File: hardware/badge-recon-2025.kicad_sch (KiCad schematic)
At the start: 73 parts, among them J1 Battery, J3 MAGSPOOF, J4 MAGSPOOF, P1 USB_C_Plug_USB2.0, Q1 DMG3415U-7, SW1 SW_Push, SW2 SW_Push, SW3 ON, SW4 SOURCE MAG, SW5 SW_Push, SW6 SW_Push, SW7 RESET, U1 PN7150B0HN_C11002E-PN7150B0HN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, U2 RP2040, U4 AP2112K-3.3, U6 W25Q16JV, U7 TC4424, Y1 27.12Mhz, Y2 12Mhz

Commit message: feat(hw): add oled in schematic
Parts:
- removed J1: Battery, Connector_PinHeader_2.54mm:PinHeader_1x02_P2.54mm_Vertical, symbol Connector:Screw_Terminal_01x02
- removed J3, J4: MAGSPOOF, Connector_PinHeader_2.54mm:PinHeader_1x02_P2.54mm_Vertical, symbol Connector_Generic:Conn_01x02
- added BT1, BT2: Battery_Cell, Battery:BatteryHolder_Keystone_2466_1xAAA, symbol Device:Battery_Cell
- added J5: OLED, Library:Display OLED 128 x32, symbol Connector:Screw_Terminal_01x04
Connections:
- net +3V3: now also J5.3 (Pin_3)
- net +BATT: now also BT2.2 (+)
- net GND: now also BT1.1 (-), J5.4 (Pin_4)
- net SCL: now also J5.2 (Pin_2)
- net SDA: now also J5.1 (Pin_1)
- net ACK_CTS: no longer names the net of U2.13 (GPIO10)
- net B_ADC: no longer names the net of U2.38 (GPIO26_ADC0)
- net CIPO_TX: no longer names the net of U2.11 (GPIO8)
- net COPI_RTS: no longer names the net of U2.14 (GPIO11)
- net CS_RX: no longer names the net of U2.12 (GPIO9)
- net LED1: no longer names the net of U2.39 (GPIO27_ADC1)
- net SWCLK: no longer names the net of U2.24 (SWCLK)
- net SWDIO: no longer names the net of U2.25 (SWD)
- new net: BT1.2 (+), BT2.1 (-)
- no-connect marks 14 -> 25
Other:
- note added: "BATTERY 2 AAA"
- note added: "OLED"
- note removed: "Missing to define which battery will be used, if 3 AAA battery or 2 Battery AA"

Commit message: feat(Hw):Update_BOM
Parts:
- removed BT1, BT2: Battery_Cell, Battery:BatteryHolder_Keystone_2466_1xAAA, symbol Device:Battery_Cell
- added J3: Battery, Footprint:BAT-TH_BH-AAA-A1AJ024, symbol Connector:Screw_Terminal_01x02
- C30, C31: LCSC# C561174 -> C107035; manf# C0603C121J5GAC -> (none)
- C34: LCSC# C466781 -> C96446; manf# C0603X5R106M160NT -> (none)
- JP1: now not fitted
- L3: manf# CONUFL001-SMD -> CONUFL001-SMD-T
- L4: footprint BomberCat:Coil_30t_30mm_0.2_0.2_0.6_0.3 -> Footprints:Coil_30t_30mm_0.2_0.2_0.6_0.3
- P1: LCSC# C2987386 -> C393939; manf# TYPE-C-31-M-31 -> (none)
- R1, R2, R20: LCSC# C169849 -> C2930027; manf# ERJ3GEYJ103V -> (none)
- R14, R21, R22: manf# WR06X104JTL -> (none)
- R4, R5: LCSC# C191782 -> C23186; manf# ERJ3RBD5101V -> (none)
- SW1, SW2, SW5, SW6: footprint (none) -> Button_Switch_SMD:SW_SPST_TL3342; LCSC# (none) -> C318889
- SW3: footprint BomberCat:JS102011SAQN -> Footprints:JS102011SAQN
- SW4: footprint BomberCat:JS202011CQN -> Footprints:JS202011CQN
- SW7: LCSC# C2886897 -> C318889
- U1: LCSC# C11002 -> C702907; manf# PN7150B0HN -> PN7150B0HN/C11002E
- U2: footprint BomberCat:RP2040-QFN-56 -> Footprints:RP2040-QFN-56
- U6: footprint BomberCat:W25Q16JVUUIQ -> Footprints:W25Q16JVUUIQ
- U7: LCSC# C636876 -> C44150
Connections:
- net +BATT: now also J3.2 (Pin_2)
- net GND: now also J3.1 (Pin_1)
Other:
- note removed: "BATTERY 2 AAA"

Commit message: feat(Hw):Init_Floorplan
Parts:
- J3: footprint Footprint:BAT-TH_BH-AAA-A1AJ024 -> Footprints:BAT-TH_BH-AAA-A1AJ024
- J5: footprint Library:Display OLED 128 x32 -> Footprints:Display OLED 128 x32
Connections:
- net CLK: no longer names the net of U1.40 (CLK_REQ)
- net GPIO1: no longer names the net of U2.28 (GPIO17)
- no-connect marks 25 -> 27
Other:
- moved on the sheet: C3, C4, C5, C6, C7, C8, C9, R1, R2, R21, R22, SW6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

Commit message: feat(Hw):Update_BOM
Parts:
- C23, C24: LCSC# C519403 -> C519507
- C25, C26: LCSC# (none) -> C107096
- C27, C28: LCSC# (none) -> C7503509
- F1: value 0.5A -> 0.75A; footprint Fuse:Fuse_0805_2012Metric -> Fuse:Fuse_0603_1608Metric; LCSC# - -> C182438; manf# MFU0805FF00500P100 -> (none)
- L3: manf# CONUFL001-SMD-T -> (none); now not fitted
- R18, R19: LCSC# C482832 -> C425452
- SW3: footprint Footprints:JS102011SAQN -> Footprints:MSK12C02; LCSC# - -> C431540; manf# JS102011SAQN -> (none)
- SW4: LCSC# (none) -> C5149820
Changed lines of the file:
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@@
 			)
 		)
+		(property "LCSC#" "C5149820"
+			(at 348.107 26.543 0)
+			(effects
+				(font
+					(size 1.27 1.27)
+				)
+				(hide yes)
+			)
+		)
 		(pin "1"
 		)
@@
 			)
 		)
-		(property "Footprint" "Footprints:JS102011SAQN"
+		(property "Footprint" "Footprints:MSK12C02"
 			(at 97.663 251.968 0)
 			(effects
@@
 			)
 		)
-		(property "LCSC#" "-"
+		(property "LCSC#" "C431540"
 			(at 97.663 251.968 0)
 			(effects
@@
 			)
 		)
-		(property "manf#" "JS102011SAQN"
+		(property "manf#" ""
 			(at 97.663 251.968 0)
 			(effects
@@
 			)
 		)
-		(property "LCSC#" "C482832"
+		(property "LCSC#" "C425452"
 			(at 205.232 52.07 0)
 			(effects
@@
 			)
 		)
-		(property "LCSC#" "C482832"
+		(property "LCSC#" "C425452"
 			(at 205.359 59.69 0)
 			(effects
@@
 			)
 		)
+		(property "LCSC#" "C7503509"
+			(at 184.15 42.926 0)
+			(effects
+				(font
+					(size 1.27 1.27)
+				)
+				(hide yes)
+			)
+		)
 		(pin "1"
 		)
@@
 			)
 		)
-		(property "Value" "0.5A"
+		(property "Value" "0.75A"
 			(at 51.308 233.8324 0)
 			(effects
@@
 			)
 		)
-		(property "Footprint" "Fuse:Fuse_0805_2012Metric"
+		(property "Footprint" "Fuse:Fuse_0603_1608Metric"
 			(at 51.308 236.22 0)
 			(effects
@@
 			)
 		)
-		(property "manf#" "MFU0805FF00500P100"
+		(property "manf#" ""
 			(at 51.308 236.22 0)
 			(effects
@@
 			)
 		)
-		(property "LCSC#" "-"
+		(property "LCSC#" "C182438"
 			(at 51.308 236.22 0)
 			(effects
@@
 			)
 		)
-		(property "LCSC#" "C519403"
+		(property "LCSC#" "C519507 "
 			(at 171.831 74.168 0)
 			(effects
@@
 		(in_bom yes)
 		(on_board yes)
-		(dnp no)
+		(dnp yes)
 		(property "Reference" "L3"
 			(at 210.185 54.102 0)
@@
 			)
 		)
-		(property "manf#" "CONUFL001-SMD-T "
+		(property "manf#" ""
 			(at 213.487 55.88 0)
 			(effects
@@
 			)
 		)
-		(property "LCSC#" "C519403"
+		(property "LCSC#" "C519507 "
 			(at 170.942 35.56 0)
 			(effects
@@
 			)
 		)
+		(property "LCSC#" "C107096"
+			(at 180.086 59.69 0)
+			(effects
+				(font
+					(size 1.27 1.27)
+				)
+				(hide yes)
+			)
+		)
 		(pin "1"
 		)
@@
 			)
 		)
+		(property "LCSC#" "C107096"
+			(at 180.086 52.197 0)
+			(effects
+				(font
+					(size 1.27 1.27)
+				)
+				(hide yes)
+			)
+		)
 		(pin "1"
 		)
@@
 			(at 184.658 67.183 0)
 			(effects
+				(font
+					(size 1.27 1.27)
+				)
+				(hide yes)
+			)
+		)
+		(property "LCSC#" "C7503509"
+			(at 184.658 67.183 0)
+			(effects

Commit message: feat(Hw): add antenna missing matching circuit
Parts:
- L3: footprint Connectors:MOLEX_1661 -> Footprints:NFC_Antenna_4T_Crossover_Final
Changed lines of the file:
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@@
 			)
 		)
-		(property "Footprint" "Connectors:MOLEX_1661"
+		(property "Footprint" "Footprints:NFC_Antenna_4T_Crossover_Final"
 			(at 213.487 55.88 0)
 			(effects

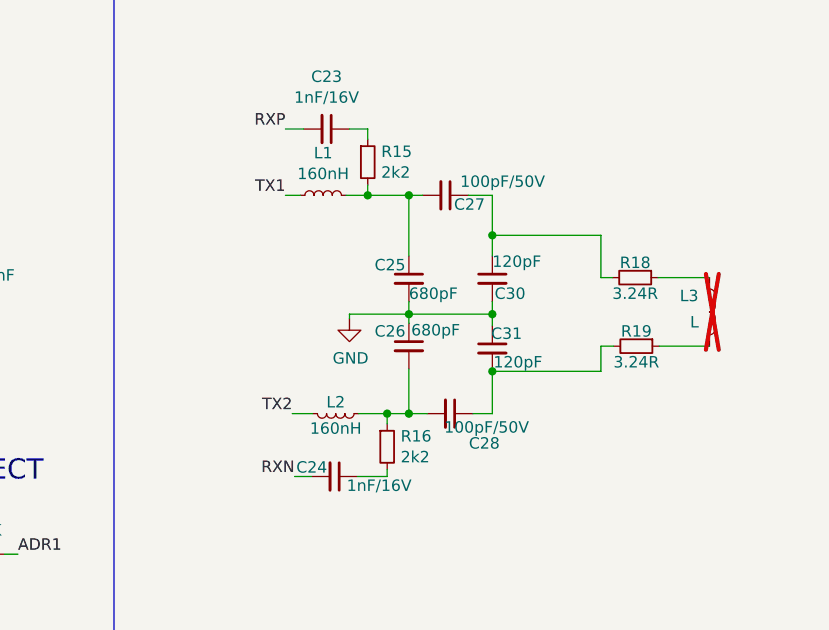
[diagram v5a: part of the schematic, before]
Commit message: feat(Hw): add ideal matching circuit
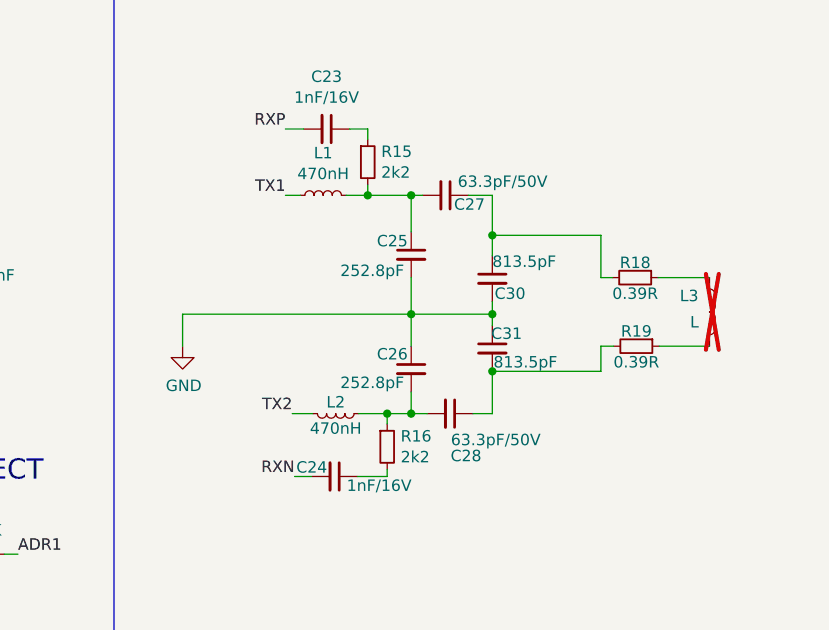
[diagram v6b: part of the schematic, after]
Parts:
- C25: value 680pF -> 252.8pF
- C26: value 680pF -> 252.8pF; LCSC# C107096 -> (none); manf# 885012206107 -> (none); provedor MOUSER -> (none)
- C27, C28: value 100pF/50V -> 63.3pF/50V; LCSC# C7503509 -> (none); manf# 06035A101JAT4A -> (none); provedor MOUSER -> (none)
- C30, C31: value 120pF -> 813.5pF; LCSC# C107035 -> (none); provedor LCSC -> (none)
- L1, L2: value 160nH -> 470nH; LCSC# C434822 -> (none); manf# MLJ1608WR16JT000 -> (none); provedor LCSC -> (none)
- R18, R19: value 3.24R -> 0.39R; LCSC# C425452 -> (none); manf# RC0603FR-073R4 -> (none); provedor LCSC -> (none)
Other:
- moved on the sheet: C25, C26

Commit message: Feat(Hw): floorplan added
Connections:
- net GND: now also P1.S1 (SHIELD)
- no-connect marks 27 -> 26
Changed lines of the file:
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@@
 	)
 	(no_connect
-		(at 22.86 274.32)
-	)
-	(no_connect
 		(at 187.96 267.97)
 	)
@@
 	(wire
 		(pts
+			(xy 22.86 274.32) (xy 22.86 276.86)
+		)
+		(stroke
+			(width 0)
+			(type default)
+		)
+	)
+	(wire
+		(pts
 			(xy 22.225 157.48) (xy 22.225 165.989)
 		)
@@
 					(unit 1)
 				)
+			)
+		)
+	)
+	(symbol
+		(lib_id "power:GND")
+		(at 22.86 276.86 0)
+		(unit 1)
+		(exclude_from_sim no)
+		(in_bom yes)
+		(on_board yes)
+		(dnp no)
+		(property "Reference" "#PWR035"
+			(at 22.86 283.21 0)
+			(effects
+				(font
+					(size 1.27 1.27)
+				)
+				(hide yes)
+			)
+		)
+		(property "Value" "GND"
+			(at 22.987 281.2542 0)
+			(effects
+				(font
+					(size 1.27 1.27)
+				)
+			)
+		)
+		(property "Footprint" ""
+			(at 22.86 276.86 0)
+			(effects
+				(font
+					(size 1.27 1.27)
+				)
+				(hide yes)
+			)
+		)
+		(property "Datasheet" ""
+			(at 22.86 276.86 0)
+			(effects
+				(font
+					(size 1.27 1.27)
+				)
+				(hide yes)
+			)
+		)
+		(property "Description" ""
+			(at 22.86 276.86 0)
+			(effects
+				(font
+					(size 1.27 1.27)
+				)
+			)
+		)
+		(pin "1"
+		)
+		(instances
+			(project "badge-recon-2025"
+				(path "/d927dcf1-a70e-4351-8ddc-20f742435b21"
+					(reference "#PWR035")
+					(unit 1)
+				)

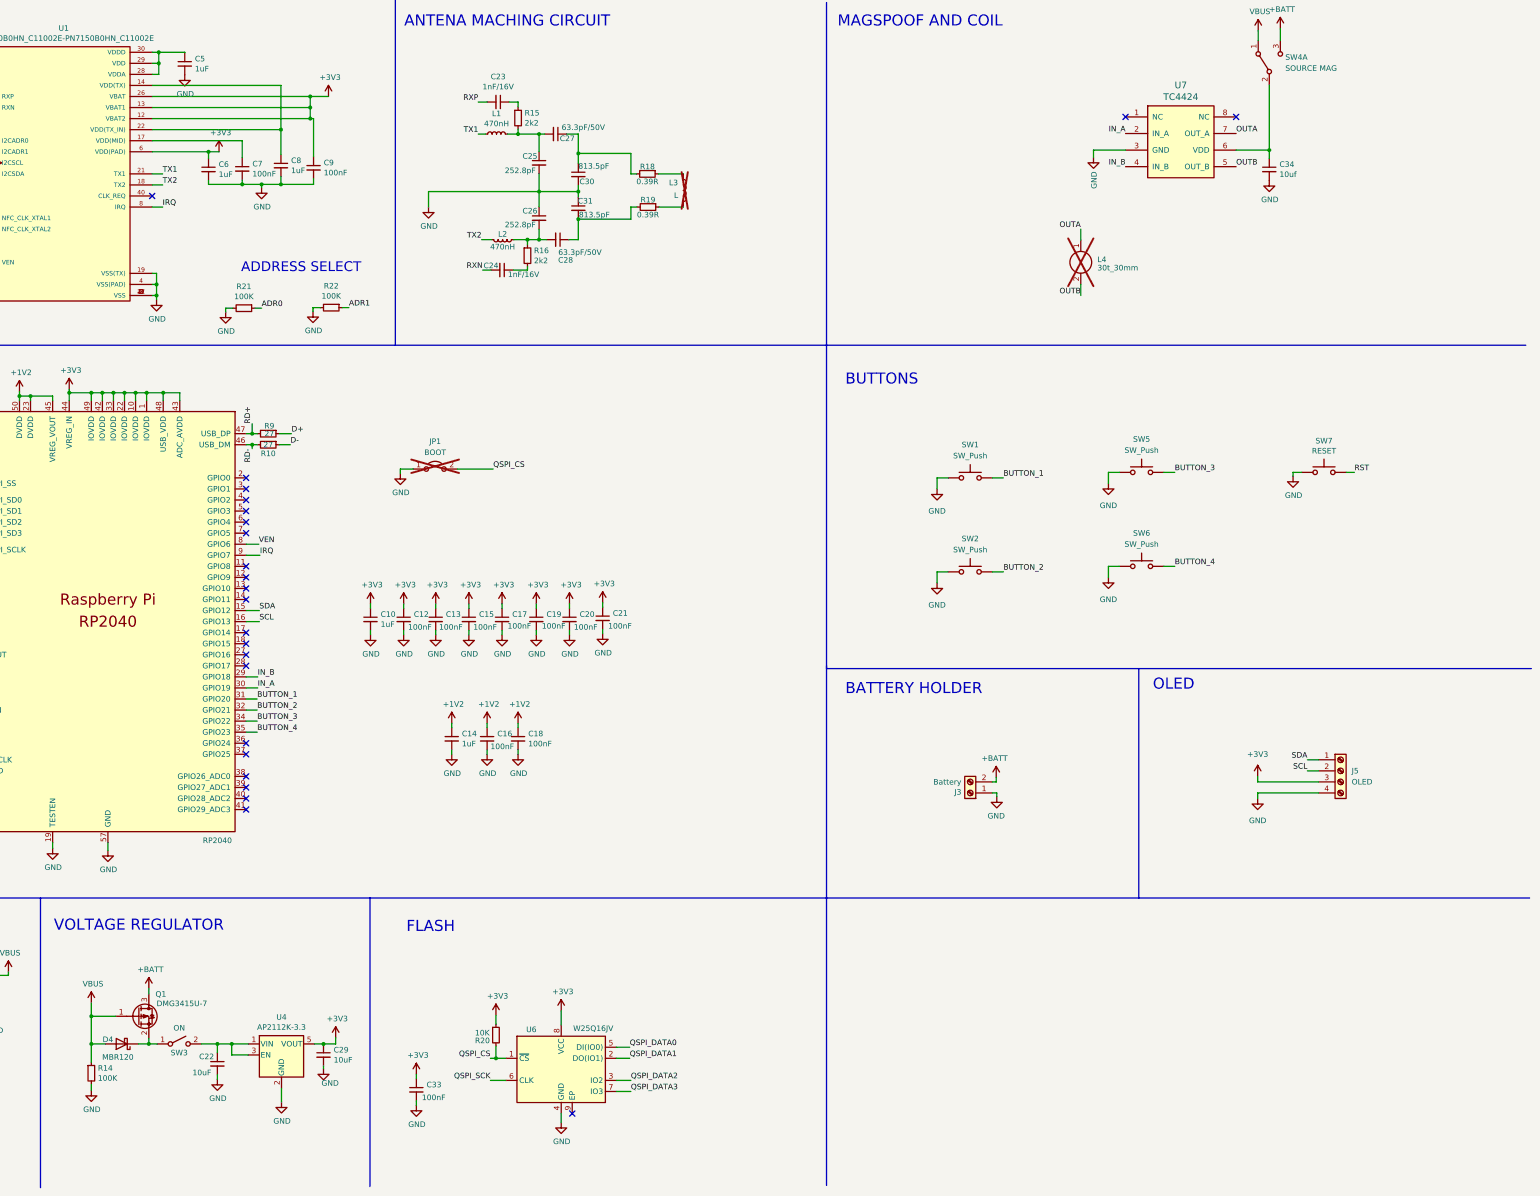
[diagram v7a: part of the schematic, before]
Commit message: feat(Hw): update part numbers for JLCPCB assembly
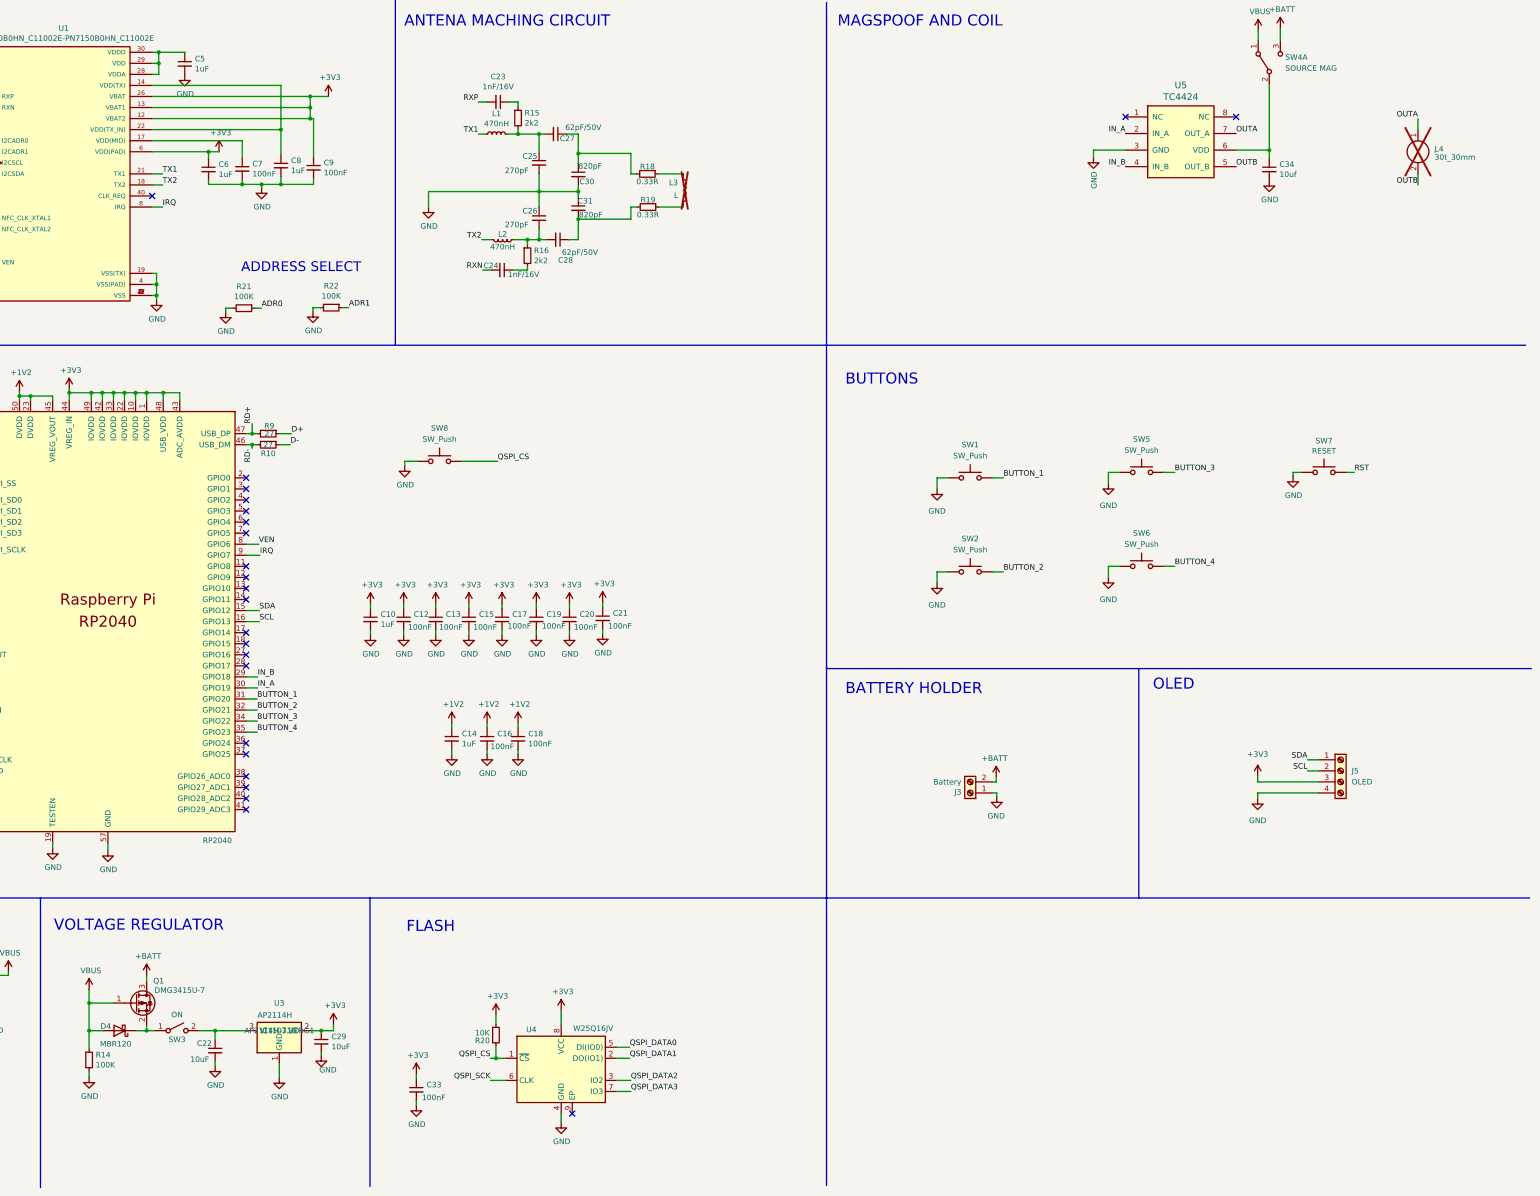
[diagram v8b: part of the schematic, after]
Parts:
- removed JP1: BOOT, Jumper:SolderJumper-2_P1.3mm_Open_TrianglePad1.0x1.5mm, symbol Jumper:Jumper_2_Open
- removed U4: AP2112K-3.3, Package_TO_SOT_SMD:SOT-23-5, symbol HunterCat-NFC-rescue:AP2112K-3.3-Regulator_Linear
- added SW8: SW_Push, Button_Switch_SMD:SW_SPST_TL3342, symbol Switch:SW_Push
- added U3: AP2114H, Package_TO_SOT_SMD:SOT-223-3_TabPin2, symbol Regulator_Linear:LD1117S33TR_SOT223
- C25: value 252.8pF -> 270pF; LCSC# C107096 -> C107046
- C26: value 252.8pF -> 270pF; LCSC# (none) -> C107046
- C27, C28: value 63.3pF/50V -> 62pF/50V; LCSC# (none) -> C282073
- C30, C31: value 813.5pF -> 820pF; LCSC# (none) -> C107057
- F1: footprint Fuse:Fuse_0603_1608Metric -> Fuse:Fuse_1812_4532Metric; LCSC# C182438 -> C3107
- L1: LCSC# (none) -> C2044483; provedor (none) -> JLCPCB
- L2: LCSC# (none) -> C2044483
- L4: LCSC# (none) -> -
- R18: value 0.39R -> 0.33R; LCSC# (none) -> C2934252; provedor (none) -> JLCPCB
- R19: value 0.39R -> 0.33R; LCSC# (none) -> C2934252; manf# (none) -> FRL0603FR330TS; provedor (none) -> JLCPCB
- U1: provedor MOUSER -> JLCPCB
- U4: renamed from U6; footprint Footprints:W25Q16JVUUIQ -> Package_SO:SOIC-8_5.3x5.3mm_P1.27mm; LCSC# (none) -> C82317; provedor MOUSER -> JLCPCB
- U5: renamed from U7; LCSC# C44150 -> TC4424AVOA
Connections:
- net +3V3: now also U3.2 (VO)
- net GND: now also SW8.1, U3.1 (GND)
- net QSPI_CS: now also SW8.2
- net at C22.1, SW3.2 (B): now also U3.3 (VI)
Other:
- moved on the sheet: C22, C29, D4, L4, Q1, R14, SW3
